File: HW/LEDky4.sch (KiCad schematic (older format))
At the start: 8 parts

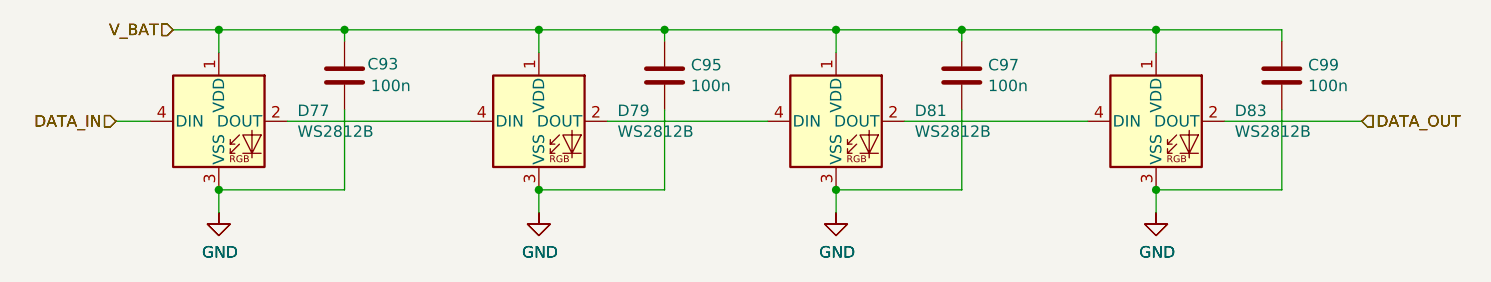
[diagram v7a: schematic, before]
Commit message: make smaller test version, start routing
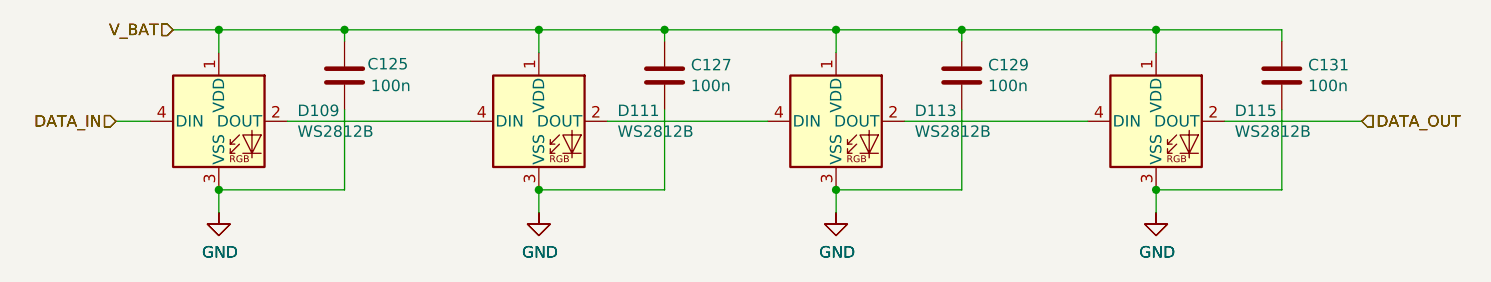
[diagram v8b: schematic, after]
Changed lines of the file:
@@
 $Descr A4 11693 8268
 encoding utf-8
-Sheet 30 44
+Sheet 30 34
 Title ""
 Date ""
@@
 AR Path="/5F79BCD0/5F79846B/5F78FD5C" Ref="#PWR0218"  Part="1"
 AR Path="/5F79BCD0/5F798482/5F78FD5C" Ref="#PWR0226"  Part="1"
-F 0 "#PWR0306" H 2150 1950 50  0001 C CNN
+F 0 "#PWR0258" H 2150 1950 50  0001 C CNN
 F 1 "GND" H 2155 2027 50  0000 C CNN
 F 2 "" H 2150 2200 50  0001 C CNN
@@
 AR Path="/5F79BCD0/5F79846B/5F78FD62" Ref="C93"  Part="1"
 AR Path="/5F79BCD0/5F798482/5F78FD62" Ref="C101"  Part="1"
-F 0 "C93" H 2800 1650 50  0000 L CNN
+F 0 "C125" H 2800 1650 50  0000 L CNN
 F 1 "100n" H 2815 1555 50  0000 L CNN
 F 2 "Capacitor_SMD:C_0402_1005Metric" H 2738 1450 50  0001 C CNN
@@
 AR Path="/5F79BCD0/5F79846B/5F78FD71" Ref="D79"  Part="1"
 AR Path="/5F79BCD0/5F798482/5F78FD71" Ref="D87"  Part="1"
-F 0 "D79" H 3894 1846 50  0000 L CNN
+F 0 "D111" H 3894 1846 50  0000 L CNN
 F 1 "WS2812B" H 3894 1755 50  0000 L CNN
 F 2 "LED_SMD:LED_WS2812B_PLCC4_5.0x5.0mm_P3.2mm" H 3600 1500 50  0001 L TNN
@@
 AR Path="/5F79BCD0/5F79846B/5F798BEB" Ref="#PWR0219"  Part="1"
 AR Path="/5F79BCD0/5F798482/5F798BEB" Ref="#PWR0227"  Part="1"
-F 0 "#PWR0307" H 3550 1950 50  0001 C CNN
+F 0 "#PWR0259" H 3550 1950 50  0001 C CNN
 F 1 "GND" H 3555 2027 50  0000 C CNN
 F 2 "" H 3550 2200 50  0001 C CNN
@@
 AR Path="/5F79BCD0/5F79846B/5F798BEE" Ref="#PWR0220"  Part="1"
 AR Path="/5F79BCD0/5F798482/5F798BEE" Ref="#PWR0228"  Part="1"
-F 0 "#PWR0308" H 4850 1950 50  0001 C CNN
+F 0 "#PWR0260" H 4850 1950 50  0001 C CNN
 F 1 "GND" H 4855 2027 50  0000 C CNN
 F 2 "" H 4850 2200 50  0001 C CNN
@@
 AR Path="/5F79BCD0/5F79846B/5F78FDA5" Ref="D83"  Part="1"
 AR Path="/5F79BCD0/5F798482/5F78FDA5" Ref="D91"  Part="1"
-F 0 "D83" H 6594 1846 50  0000 L CNN
+F 0 "D115" H 6594 1846 50  0000 L CNN
 F 1 "WS2812B" H 6594 1755 50  0000 L CNN
 F 2 "LED_SMD:LED_WS2812B_PLCC4_5.0x5.0mm_P3.2mm" H 6300 1500 50  0001 L TNN
@@
 AR Path="/5F79BCD0/5F79846B/5F78FDAB" Ref="#PWR0221"  Part="1"
 AR Path="/5F79BCD0/5F798482/5F78FDAB" Ref="#PWR0229"  Part="1"
-F 0 "#PWR0309" H 6250 1950 50  0001 C CNN
+F 0 "#PWR0261" H 6250 1950 50  0001 C CNN
 F 1 "GND" H 6255 2027 50  0000 C CNN
 F 2 "" H 6250 2200 50  0001 C CNN
@@
 AR Path="/5F79BCD0/5F79846B/5F78FDB1" Ref="C99"  Part="1"
 AR Path="/5F79BCD0/5F798482/5F78FDB1" Ref="C107"  Part="1"
-F 0 "C99" H 6915 1646 50  0000 L CNN
+F 0 "C131" H 6915 1646 50  0000 L CNN
 F 1 "100n" H 6915 1555 50  0000 L CNN
 F 2 "Capacitor_SMD:C_0402_1005Metric" H 6838 1450 50  0001 C CNN
@@
 AR Path="/5F79BCD0/5F79846B/5F78FD56" Ref="D77"  Part="1"
 AR Path="/5F79BCD0/5F798482/5F78FD56" Ref="D85"  Part="1"
-F 0 "D77" H 2494 1846 50  0000 L CNN
+F 0 "D109" H 2494 1846 50  0000 L CNN
 F 1 "WS2812B" H 2494 1755 50  0000 L CNN
 F 2 "LED_SMD:LED_WS2812B_PLCC4_5.0x5.0mm_P3.2mm" H 2200 1500 50  0001 L TNN
@@
 AR Path="/5F79BCD0/5F79846B/5F798BE8" Ref="#PWR0222"  Part="1"
 AR Path="/5F79BCD0/5F798482/5F798BE8" Ref="#PWR0230"  Part="1"
-F 0 "#PWR0310" H 2150 1950 50  0001 C CNN
+F 0 "#PWR0262" H 2150 1950 50  0001 C CNN
 F 1 "GND" H 2155 2027 50  0000 C CNN
 F 2 "" H 2150 2200 50  0001 C CNN
@@
 AR Path="/5F79BCD0/5F79846B/5F78FD77" Ref="#PWR0223"  Part="1"
 AR Path="/5F79BCD0/5F798482/5F78FD77" Ref="#PWR0231"  Part="1"
-F 0 "#PWR0311" H 3550 1950 50  0001 C CNN
+F 0 "#PWR0263" H 3550 1950 50  0001 C CNN
 F 1 "GND" H 3555 2027 50  0000 C CNN
 F 2 "" H 3550 2200 50  0001 C CNN
@@
 AR Path="/5F79BCD0/5F79846B/5F78FD7D" Ref="C95"  Part="1"
 AR Path="/5F79BCD0/5F798482/5F78FD7D" Ref="C103"  Part="1"
-F 0 "C95" H 4215 1646 50  0000 L CNN
+F 0 "C127" H 4215 1646 50  0000 L CNN
 F 1 "100n" H 4215 1555 50  0000 L CNN
 F 2 "Capacitor_SMD:C_0402_1005Metric" H 4138 1450 50  0001 C CNN
@@
 AR Path="/5F79BCD0/5F79846B/5F78FD8B" Ref="D81"  Part="1"
 AR Path="/5F79BCD0/5F798482/5F78FD8B" Ref="D89"  Part="1"
-F 0 "D81" H 5194 1846 50  0000 L CNN
+F 0 "D113" H 5194 1846 50  0000 L CNN
 F 1 "WS2812B" H 5194 1755 50  0000 L CNN
 F 2 "LED_SMD:LED_WS2812B_PLCC4_5.0x5.0mm_P3.2mm" H 4900 1500 50  0001 L TNN
@@
 AR Path="/5F79BCD0/5F79846B/5F78FD91" Ref="#PWR0224"  Part="1"
 AR Path="/5F79BCD0/5F798482/5F78FD91" Ref="#PWR0232"  Part="1"
-F 0 "#PWR0312" H 4850 1950 50  0001 C CNN
+F 0 "#PWR0264" H 4850 1950 50  0001 C CNN
 F 1 "GND" H 4855 2027 50  0000 C CNN
 F 2 "" H 4850 2200 50  0001 C CNN
@@
 AR Path="/5F79BCD0/5F79846B/5F78FD97" Ref="C97"  Part="1"
 AR Path="/5F79BCD0/5F798482/5F78FD97" Ref="C105"  Part="1"
-F 0 "C97" H 5515 1646 50  0000 L CNN
+F 0 "C129" H 5515 1646 50  0000 L CNN
 F 1 "100n" H 5515 1555 50  0000 L CNN
 F 2 "Capacitor_SMD:C_0402_1005Metric" H 5438 1450 50  0001 C CNN
@@
 AR Path="/5F79BCD0/5F79846B/5F798BF1" Ref="#PWR0225"  Part="1"
 AR Path="/5F79BCD0/5F798482/5F798BF1" Ref="#PWR0233"  Part="1"
-F 0 "#PWR0313" H 6250 1950 50  0001 C CNN
+F 0 "#PWR0265" H 6250 1950 50  0001 C CNN
 F 1 "GND" H 6255 2027 50  0000 C CNN
 F 2 "" H 6250 2200 50  0001 C CNN
